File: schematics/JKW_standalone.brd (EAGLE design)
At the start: 159.4 x 80.7 mm, 217 parts, among them IC1 4093D, IC2 AT-MEGA-8L, IC4 ATMEGA2560-16AU, Q1 BSS84, Q10 BSS84, Q11 BSS84, Q2 BSS84, Q3 BSS84, Q4 BSS84, Q5 BSS84, Q6 BSS84, Q7 BSS84, Q8 BSS84, Q9 BSS84, T1 Mouser: 771-2N7002BK215 , N-C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, T10 Mouser: 771-2N7002BK215 , N-C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, T11 Mouser: 771-2N7002BK215 , N-C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, T12 Mouser: 771-2N7002BK215 , N-C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, T2 Mouser: 771-2N7002BK215 , N-C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, T3 Mouser: 771-2N7002BK215 , N-C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, T4 T-IRLMS6702, T5 Mouser: 771-2N7002BK215 , N-C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, T6 Mouser: 771-2N7002BK215 , N-C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, T7 Mouser: 771-2N7002BK215 , N-C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, T8 Mouser: 771-2N7002BK215 , N-C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, T9 Mouser: 771-2N7002BK215 , N-C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

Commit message: ATm8 update: increased number of waiting steps to start 'go_back'
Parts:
- added PE: 100nF, RCLDT:0805
- R_REED_DOWN: value 5k / n.b. (Reed) -> 5k / n.b. (Reed / 5V Honda Signal)
- R_REED_UP: value n.b. / 5k (Reed) -> n.b.(Honda Signal) / 5k (Reed)
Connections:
- net GND: now also PE.1
- net VDD: now also PE.2
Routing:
- net VDD: track 749.9 -> 752.7 mm
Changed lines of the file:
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@@
 <attribute name="NAME" x="133.9325" y="43.2975" size="0.6096" layer="26" rot="MR90"/>
 </element>
-<element name="R_REED_DOWN" library="RCLDT" package="0805" value="5k / n.b. (Reed)" x="33.5" y="17.525" smashed="yes" rot="R90">
+<element name="R_REED_DOWN" library="RCLDT" package="0805" value="5k / n.b. (Reed / 5V Honda Signal)" x="33.5" y="17.525" smashed="yes" rot="R90">
 <attribute name="NAME" x="33.4325" y="15.7275" size="0.6096" layer="25" rot="R270"/>
 </element>
@@
 <element name="D8" library="diode" package="SOT23" value="5.5V" x="17.3" y="36.5" rot="R180"/>
 <element name="D12" library="diode" package="SOD80C" value="20V-Zdiode" x="67.6" y="17.3" rot="R180"/>
-<element name="R_REED_UP" library="RCLDT" package="0805" value="n.b. / 5k (Reed)" x="31.8" y="17.5" smashed="yes" rot="R270">
+<element name="R_REED_UP" library="RCLDT" package="0805" value="n.b.(Honda Signal) / 5k (Reed)" x="31.8" y="17.5" smashed="yes" rot="R270">
 <attribute name="NAME" x="31.6825" y="15.7525" size="0.6096" layer="25" rot="R270"/>
 <attribute name="VALUE" x="30.1825" y="20.1525" size="0.6096" layer="27" rot="R270"/>
@@
 <element name="Q10" library="transistor-small-signal" package="SOT23" value="BSS84" x="97.5" y="62.3" rot="MR90"/>
 <element name="Q11" library="transistor-small-signal" package="SOT23" value="BSS84" x="119.7" y="71.4" rot="R270"/>
+<element name="PE" library="RCLDT" package="0805" value="100nF" x="99.2" y="40.4" rot="MR90"/>
 </elements>
 <signals>
@@
 <contactref element="U$19" pad="17"/>
 <via x="117.525" y="53.775" extent="1-16" drill="0.3"/>
+<contactref element="PE" pad="1"/>
+<wire x1="149.816" y1="40.8" x2="145.9937" y2="43.1607" width="0" layer="19" extent="1-16"/>
 </signal>
 <signal name="DZ">
@@
 <wire x1="83.5" y1="7.8" x2="84.9" y2="9.2" width="0.254" layer="16"/>
 <wire x1="84.9" y1="9.2" x2="84.9" y2="15.2" width="0.254" layer="16"/>
-<wire x1="85.1" y1="22.8" x2="85.4" y2="23.1" width="0.254" layer="1"/>
 <wire x1="84.8" y1="15.1" x2="84.9" y2="15.2" width="0.254" layer="1"/>
 <via x="84.9" y="15.2" extent="1-16" drill="0.3"/>
@@
 <wire x1="84.9" y1="21.3" x2="85.1" y2="21.5" width="0.254" layer="16"/>
 <via x="85.1" y="21.5" extent="1-16" drill="0.3"/>
-<wire x1="85.1" y1="21.5" x2="85.9" y2="22.3" width="0.254" layer="1"/>
-<wire x1="85.9" y1="22.3" x2="85.9" y2="22.75" width="0.254" layer="1"/>
 <wire x1="71.1" y1="41.4" x2="72.8" y2="39.7" width="0.254" layer="1"/>
 <wire x1="72.8" y1="39.7" x2="72.8" y2="38.7" width="0.254" layer="1"/>
@@
 <wire x1="90.9" y1="62.2" x2="92.3" y2="62.2" width="0.254" layer="16"/>
 <wire x1="92.3" y1="62.2" x2="92.5" y2="62.4" width="0.254" layer="16"/>
-<wire x1="85.9" y1="22.75" x2="85.4" y2="23.1" width="0" layer="19" extent="1-1"/>
+<contactref element="PE" pad="2"/>
+<wire x1="99.2" y1="41.416" x2="99.616" y2="41.416" width="0.254" layer="16"/>
+<wire x1="99.616" y1="41.416" x2="100.595" y2="42.395" width="0.254" layer="16"/>
+<wire x1="100.595" y1="43.8708" x2="100.595" y2="42.395" width="0.254" layer="16"/>
+<wire x1="85.9" y1="22.75" x2="85.9" y2="22.3" width="0.254" layer="1"/>
+<wire x1="85.9" y1="22.3" x2="85.1" y2="21.5" width="0.254" layer="1"/>
 </signal>
 <signal name="TX0">
@@
 <wire x1="87" y1="59.4" x2="88" y2="59.4" width="0.254" layer="1"/>
 <wire x1="88" y1="59.4" x2="88.4" y2="59.8" width="0.254" layer="1"/>
-<wire x1="88.4" y1="59.8" x2="120.6" y2="59.8" width="0.254" layer="1"/>
-<wire x1="120.6" y1="59.8" x2="120.7" y2="59.7" width="0.254" layer="1"/>
-<wire x1="120.7" y1="59.7" x2="121.6" y2="59.7" width="0.254" layer="1"/>
-<wire x1="121.6" y1="59.7" x2="121.7" y2="59.8" width="0.254" layer="1"/>
-<wire x1="121.7" y1="59.8" x2="139.1" y2="59.8" width="0.254" layer="1"/>
+<wire x1="88.4" y1="59.8" x2="139.1" y2="59.8" width="0.254" layer="1"/>
 <wire x1="139.1" y1="59.8" x2="139.5" y2="59.4" width="0.254" layer="1"/>
 </signal>
@@
 <wire x1="87.4" y1="60.4" x2="87.4" y2="60.3" width="0.254" layer="16"/>
 <via x="87.4" y="60.4" extent="1-16" drill="0.3"/>
-<wire x1="87.4" y1="60.4" x2="121.2" y2="60.4" width="0.254" layer="1"/>
+<wire x1="87.4" y1="60.4" x2="121" y2="60.4" width="0.254" layer="1"/>
+<wire x1="121" y1="60.4" x2="121.2" y2="60.6" width="0.254" layer="1"/>
 <contactref element="T9" pad="1"/>
 <wire x1="134.1474" y1="64.0113" x2="134.1474" y2="64.1526" width="0.254" layer="16"/>
@@
 <wire x1="133" y1="65.3" x2="121.2" y2="65.3" width="0.254" layer="1"/>
 <via x="121.2" y="65.3" extent="1-16" drill="0.3"/>
-<wire x1="121.2" y1="65.3" x2="121.2" y2="60.4" width="0.254" layer="16"/>
-<via x="121.2" y="60.4" extent="1-16" drill="0.3"/>
+<wire x1="121.2" y1="65.3" x2="121.2" y2="60.6" width="0.254" layer="16"/>
+<via x="121.2" y="60.6" extent="1-16" drill="0.3"/>
 </signal>
 <signal name="D46">

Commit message: added pull down for dimm transistors
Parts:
- added R_B_LED_12, R_B_LED_13, R_B_LED_14, R_B_LED_15: 10k, RCLDT:0805
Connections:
- net D13: now also R_B_LED_12.1
- net D7: now also R_B_LED_15.1
- net D8: now also R_B_LED_14.1
- net D9: now also R_B_LED_13.1
- net GND: now also R_B_LED_12.2, R_B_LED_13.2, R_B_LED_14.2, R_B_LED_15.2
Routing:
- net D8: track 72.1 -> 76.4 mm
- net D7: track 101.1 -> 103.0 mm
- net D13: track 84.0 -> 85.6 mm
- net D9: track 68.8 -> 69.8 mm
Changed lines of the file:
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@@
 <?xml version="1.0" encoding="utf-8"?>
 <!DOCTYPE eagle SYSTEM "eagle.dtd">
-<eagle version="6.2">
+<eagle version="6.1">
 <drawing>
 <settings>
@@
 <element name="Q11" library="transistor-small-signal" package="SOT23" value="BSS84" x="119.7" y="71.4" rot="R270"/>
 <element name="PE" library="RCLDT" package="0805" value="100nF" x="99.2" y="40.4" rot="MR90"/>
+<element name="R_B_LED_12" library="RCLDT" package="0805" value="10k" x="113.7" y="41.3" rot="MR270"/>
+<element name="R_B_LED_13" library="RCLDT" package="0805" value="10k" x="79" y="40.1" rot="MR270"/>
+<element name="R_B_LED_14" library="RCLDT" package="0805" value="10k" x="88.9" y="46.1" rot="MR180"/>
+<element name="R_B_LED_15" library="RCLDT" package="0805" value="10k" x="103.1" y="54.2"/>
 </elements>
 <signals>
@@
 <via x="117.525" y="53.775" extent="1-16" drill="0.3"/>
 <contactref element="PE" pad="1"/>
+<contactref element="R_B_LED_12" pad="2"/>
+<contactref element="R_B_LED_13" pad="2"/>
+<contactref element="R_B_LED_14" pad="2"/>
+<contactref element="R_B_LED_15" pad="2"/>
 <wire x1="149.816" y1="40.8" x2="145.9937" y2="43.1607" width="0" layer="19" extent="1-16"/>
 </signal>
@@
 <wire x1="97.1776" y1="54.8113" x2="97.1776" y2="55.7224" width="0.254" layer="1"/>
 <wire x1="97.1776" y1="55.7224" x2="97" y2="55.9" width="0.254" layer="1"/>
+<contactref element="R_B_LED_15" pad="1"/>
+<wire x1="102.084" y1="54.2" x2="101.0639" y2="54.2" width="0.254" layer="1"/>
+<wire x1="101.0639" y1="54.2" x2="100.4526" y2="54.8113" width="0.254" layer="1"/>
 </signal>
 <signal name="D8">
@@
 <wire x1="82.55" y1="43.05" x2="83.1" y2="42.5" width="0.254" layer="1"/>
 <wire x1="83.1" y1="42.5" x2="84.9" y2="42.5" width="0.254" layer="16"/>
+<contactref element="R_B_LED_14" pad="1"/>
+<wire x1="87.884" y1="46.1" x2="85.8" y2="46.1" width="0.254" layer="16"/>
+<wire x1="85.8" y1="46.1" x2="85.6" y2="45.9" width="0.254" layer="16"/>
+<wire x1="85.6" y1="45.9" x2="85.6" y2="45.5" width="0.254" layer="16"/>
+<wire x1="85.6" y1="45.5" x2="85.3" y2="45.2" width="0.254" layer="16"/>
+<wire x1="85.3" y1="45.2" x2="85.3" y2="44.1861" width="0.254" layer="16"/>
+<wire x1="85.3" y1="44.1861" x2="85.2026" y2="44.0887" width="0.254" layer="16"/>
 </signal>
 <signal name="D9">
@@
 <wire x1="81" y1="47.6" x2="81" y2="48.3861" width="0.254" layer="16"/>
 <wire x1="81" y1="48.3861" x2="81.1026" y2="48.4887" width="0.254" layer="16"/>
+<contactref element="R_B_LED_13" pad="1"/>
+<wire x1="79" y1="41.116" x2="79" y2="42.2" width="0.254" layer="16"/>
 </signal>
 <signal name="D39">
@@
 <wire x1="103.8" y1="43.1" x2="114.8" y2="43.1" width="0.254" layer="1"/>
 <wire x1="114.8" y1="43.1" x2="115.2" y2="42.7" width="0.254" layer="1"/>
+<contactref element="R_B_LED_12" pad="1"/>
+<wire x1="113.7" y1="42.316" x2="114.816" y2="42.316" width="0.254" layer="16"/>
+<wire x1="114.816" y1="42.316" x2="115.2" y2="42.7" width="0.254" layer="16"/>
 </signal>
 <signal name="D22">

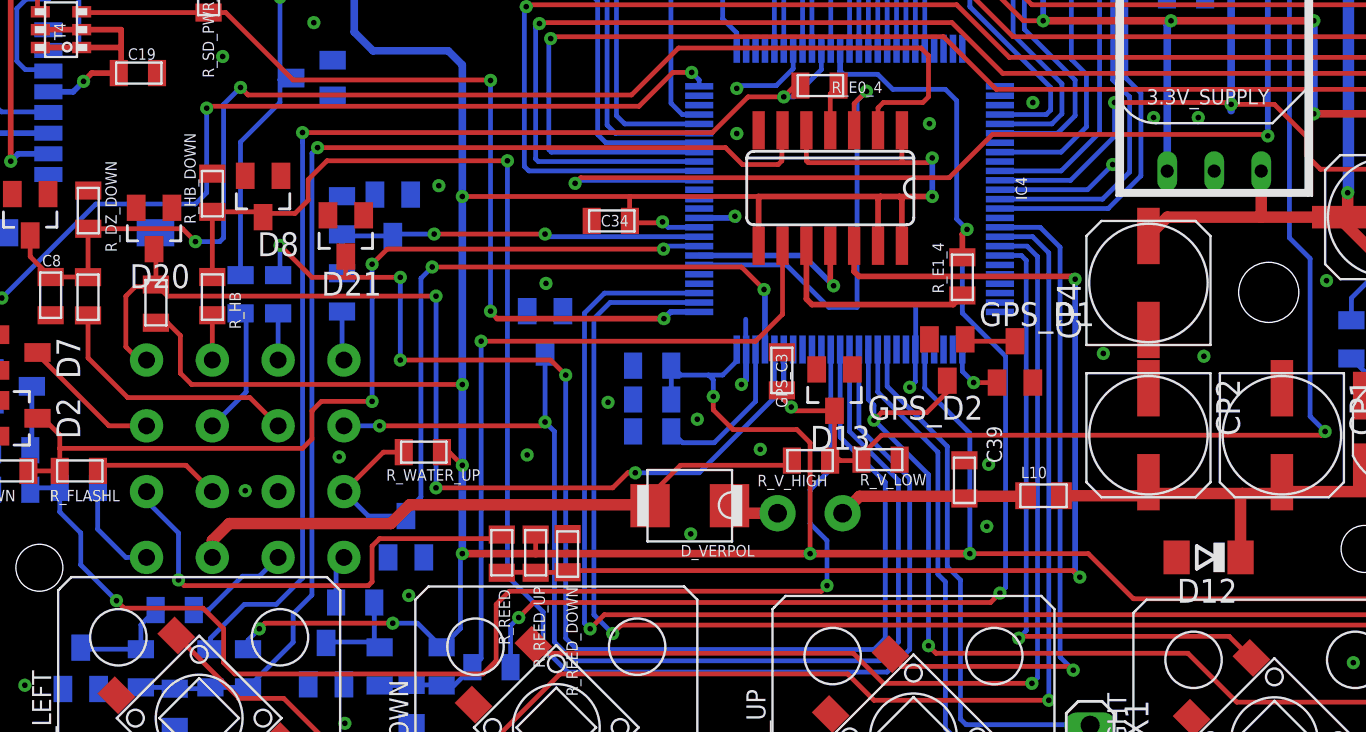
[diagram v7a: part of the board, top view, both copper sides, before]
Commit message: improved overvoltage schematic
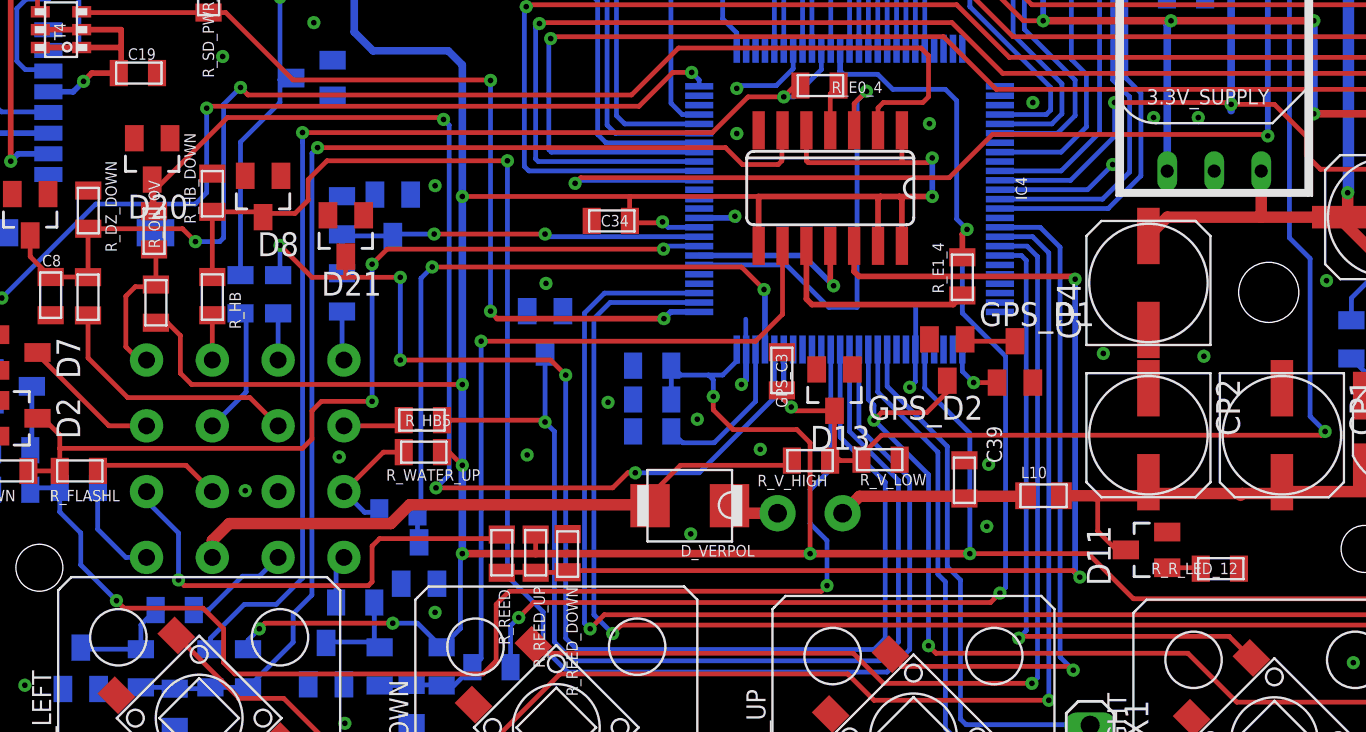
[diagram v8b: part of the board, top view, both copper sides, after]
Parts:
- removed D12: 20V-Zdiode, diode:SOD80C
- added D11: 20V-Zdiode, diode:SOT23
- added R_HB5: 600R, RCLDT:0805
- added R_OIL_OV, R_OIL_OV1: 1k, RCLDT:0805
- added R_R_LED_12: 220R, RCLDT:0805
- C35: value 22p -> 100nF
- C5, C7: value 100nF -> 22pF
- moved D20 3.70 mm to (11.4, 38.5)
- moved D3 1.57 mm to (25.6, 17.0)
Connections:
- new net N$109: D11.1, R_R_LED_12.2
- new net N$110: R_HB5.1, SPEEDOSTECKER.P$5
- new net N$111: R_OIL_OV1.1, R_WATER_UP.2, SPEEDOSTECKER.P$12
- new net N999: R_OIL_OV.1, R_OIL_UP.1, SPEEDOSTECKER.P$2
- net A0: now also R_OIL_OV1.2; no longer R_WATER_UP.2, SPEEDOSTECKER.P$12
- net A1: now also R_OIL_OV.2; no longer R_OIL_UP.1, SPEEDOSTECKER.P$2
- net GND: now also R_R_LED_12.1; no longer D12.A
- net N$1: now also D11.3; no longer D12.C
- net NG_IN: now also R_HB5.2; no longer SPEEDOSTECKER.P$5
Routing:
- net N999: track 0.00 -> 7.85 mm
- net A0: track 43.4 -> 36.4 mm
- net A1: track 55.8 -> 62.4 mm
- net N$111: track 0.00 -> 6.63 mm
- net NG_IN: track 62.3 -> 57.0 mm, vias 2 -> 1
- net N$110: track 0.00 -> 3.31 mm
- net N$109: track 0.00 -> 1.80 mm
- net N$1: track 23.3 -> 23.9 mm
